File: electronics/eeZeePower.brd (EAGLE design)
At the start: 20.3 x 11.6 mm, 10 parts

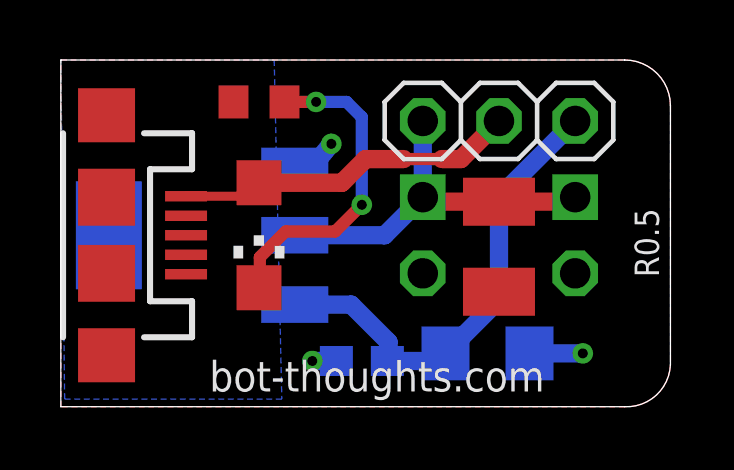
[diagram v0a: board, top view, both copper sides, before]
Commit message: updated microb footprint with new library version, added shielding to ground, fixed missing junction
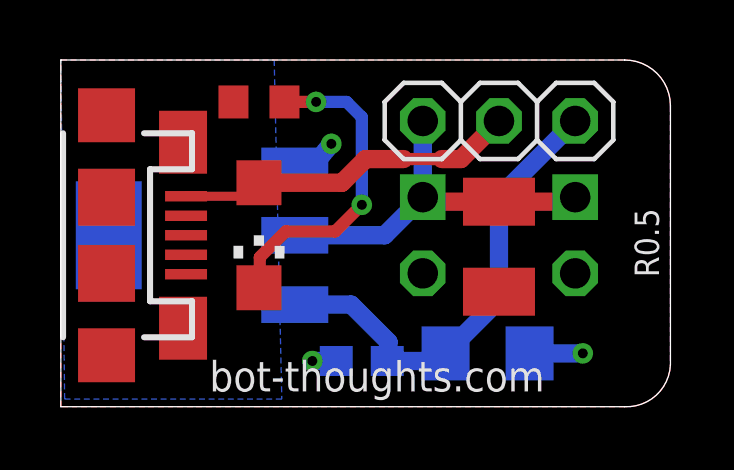
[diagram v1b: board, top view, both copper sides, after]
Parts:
- JP1: device SparkFun-Connectors:USB-MICROB -> bt_electromech:USB-MICROB
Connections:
- net GND: now also JP1.MT3, JP1.MT4
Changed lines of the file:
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@@
 <attribute name="VALUE" x="20.32" y="8.255" size="1.27" layer="28" rot="MR270"/>
 </element>
-<element name="JP1" library="SparkFun-Connectors" package="USB-MICROB" value="USB-MICROB" x="1.524" y="5.715" smashed="yes" rot="R270">
-<attribute name="PROD_ID" value="CONN-09505" x="1.524" y="5.715" size="1.778" layer="27" rot="R270" display="off"/>
-</element>
+<element name="JP1" library="bt_electromech" package="USB-MICROB" value="USB-MICROB" x="1.524" y="5.715" smashed="yes" rot="R270"/>
 </elements>
 <signals>
@@
 <contactref element="R1" pad="1"/>
 <contactref element="JP1" pad="GND"/>
-<contactref element="JP1" pad="MT2"/>
-<contactref element="JP1" pad="MT1"/>
 <wire x1="9.183" y1="1.524" x2="8.382" y2="1.524" width="0.6096" layer="16"/>
 <wire x1="15.624" y1="1.778" x2="17.399" y2="1.778" width="0.6096" layer="16"/>
@@
 <wire x1="8.4074" y1="8.0264" x2="9.017" y2="8.763" width="0.6096" layer="16"/>
 <via x="9.017" y="8.763" extent="1-16" drill="0.3302"/>
+<contactref element="JP1" pad="MT2"/>
+<contactref element="JP1" pad="MT3"/>
+<contactref element="JP1" pad="MT4"/>
+<contactref element="JP1" pad="MT1"/>
 </signal>
 <signal name="N$5">

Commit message: added value to resistor, removed silk value
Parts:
- R1: value (none) -> 330
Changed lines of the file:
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@@
 <element name="C2" library="rcl" package="C0603" value="0.1uF" x="10.033" y="1.524" smashed="yes" rot="MR0"/>
 <element name="C4" library="rcl" package="SMC_B" value="100uF" x="14.605" y="5.334" smashed="yes" rot="R270"/>
-<element name="R1" library="resistor" package="R0603" value="" x="6.604" y="10.16" smashed="yes">
-<attribute name="VALUE" x="5.715" y="8.128" size="1.27" layer="27"/>
-</element>
+<element name="R1" library="resistor" package="R0603" value="330" x="6.604" y="10.16" smashed="yes"/>
 <element name="C1" library="rcl" package="C1206" value="10uF" x="14.224" y="1.778" smashed="yes" rot="MR180"/>
 <element name="JP3" library="pinhead-2" package="1X02-S" value="" x="12.065" y="5.715" smashed="yes" rot="MR270">
